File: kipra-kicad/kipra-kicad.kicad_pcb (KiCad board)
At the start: 2 copper layers, 128.2 x 134.8 mm, 51 parts

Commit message: add silkscreen text
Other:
- board text added: "k i p r a"
- board text added: "kipra v1 (2024-04) by Peter Lyons (focusaurus) It's kinda pragmatic."

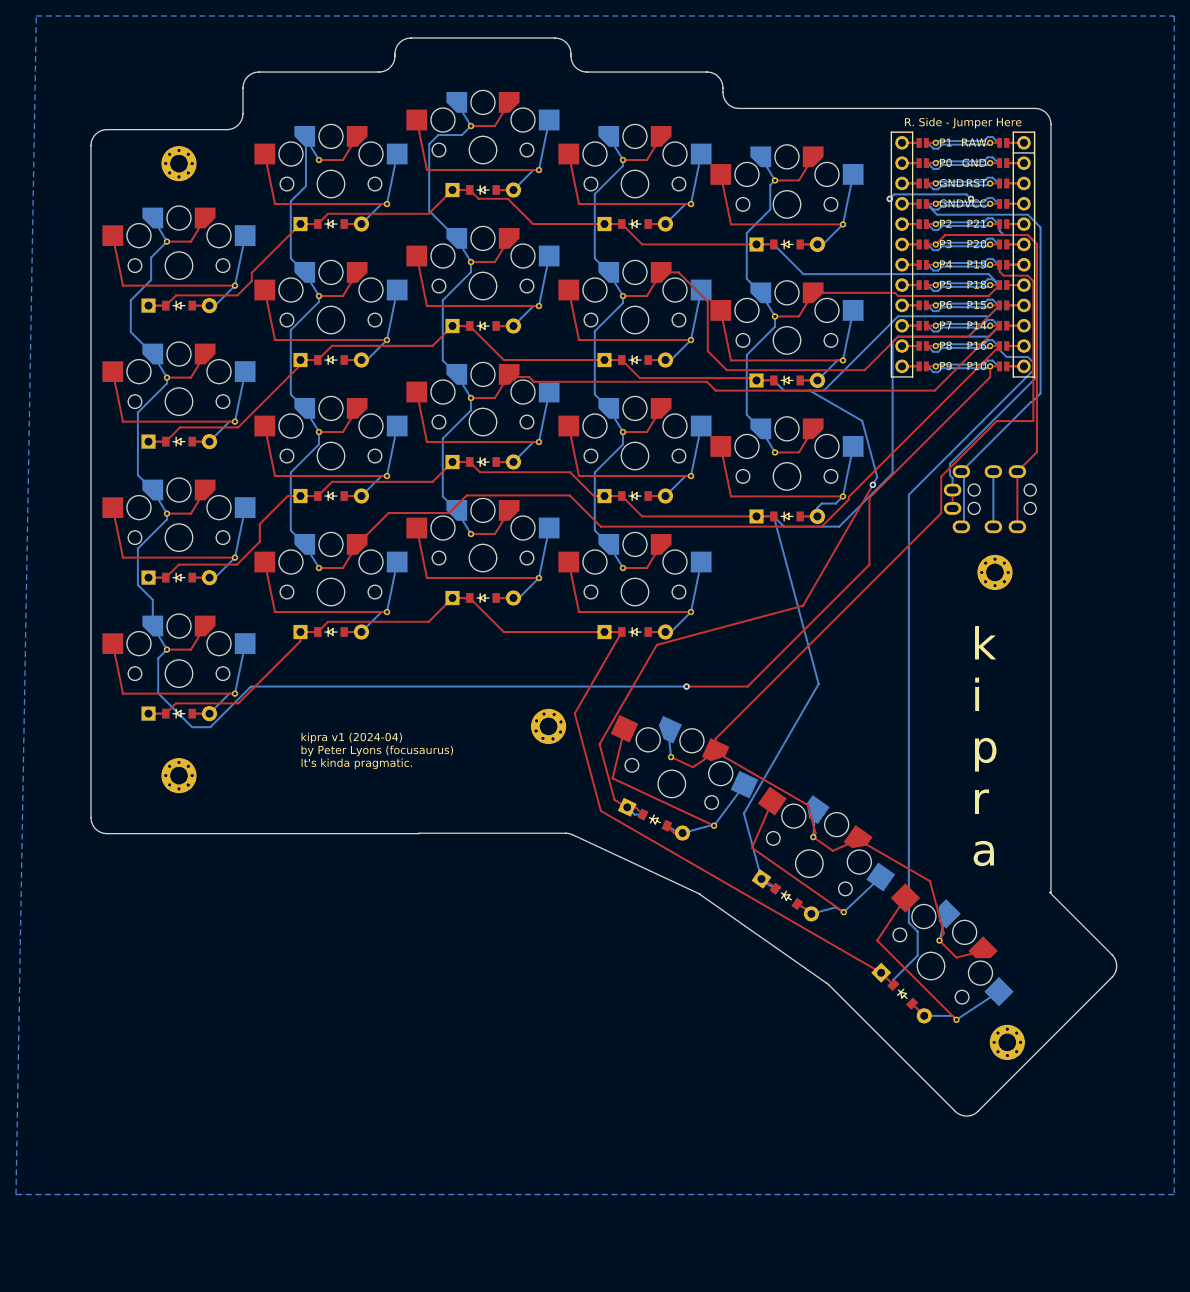
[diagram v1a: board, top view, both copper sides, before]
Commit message: added a reset button (ergogen redo)
Had to go back to ergogen. Will need to redo all the traces now.
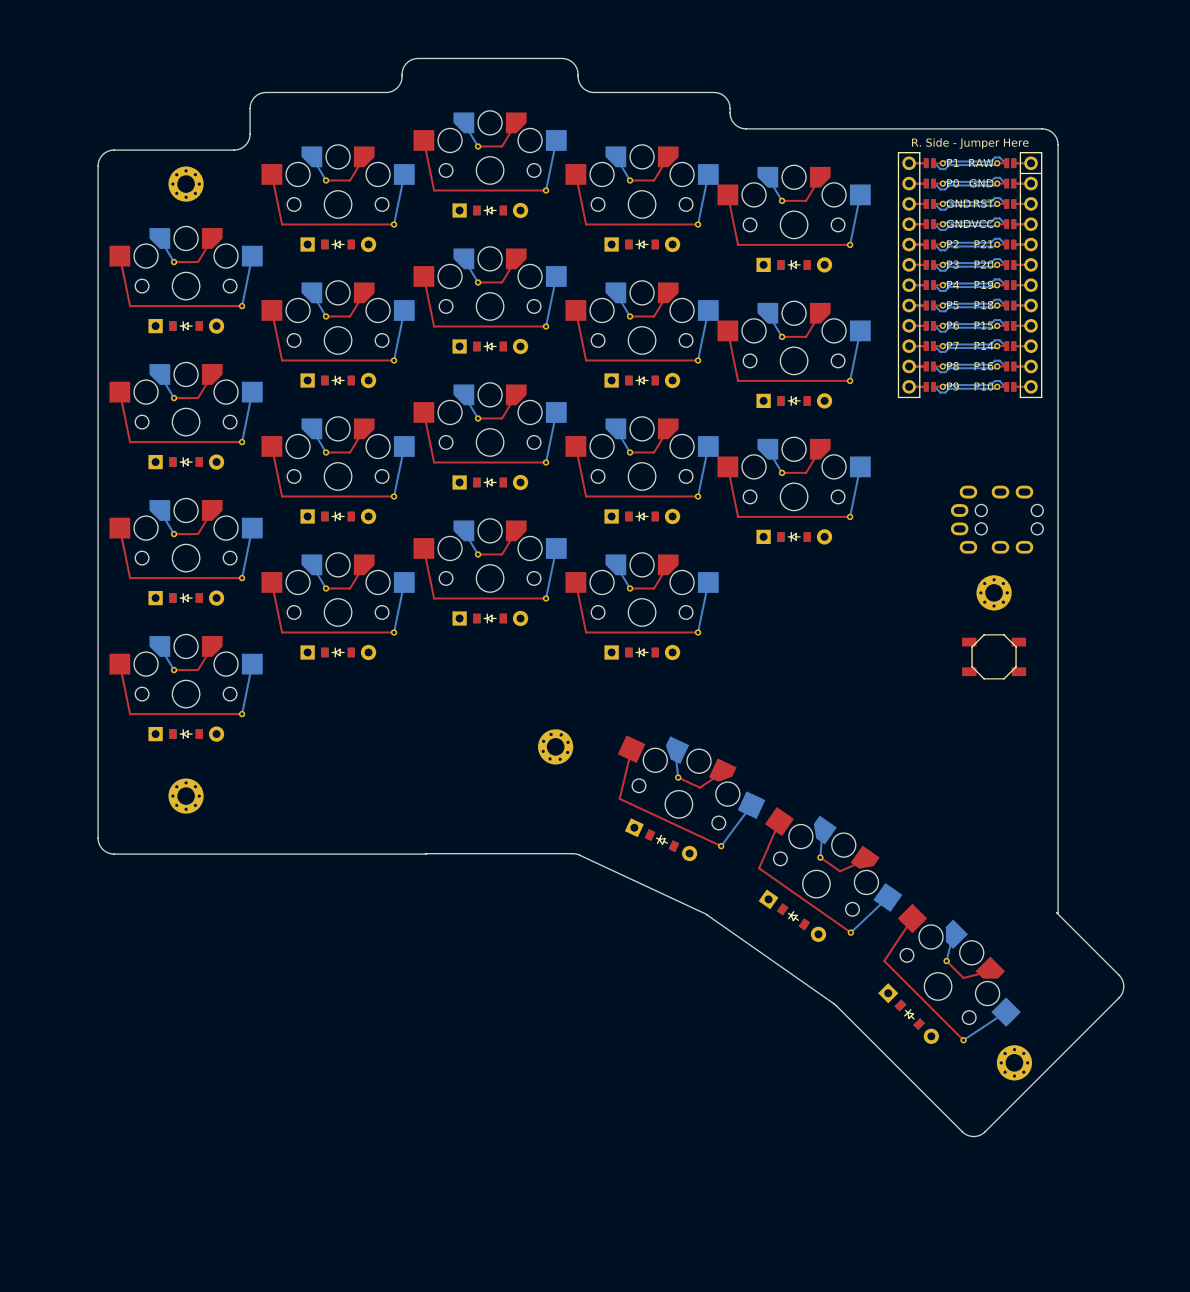
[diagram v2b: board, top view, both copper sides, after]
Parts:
- added B1: , E73:SW_TACT_ALPS_SKQGABE010, F.Cu at (201.0, 95.3)
- moved D16 2.71 mm to (157.0, 43.8)
- moved MCU1 2.71 mm to (198.0, 46.3)
- moved D11 2.71 mm to (138.0, 56.5)
- moved D15 2.71 mm to (157.0, 60.8)
- moved D2 2.71 mm to (100.0, 88.0)
- moved S17 2.71 mm to (176.0, 75.3)
- moved S6 2.71 mm to (119.0, 72.8)
- moved S3 2.71 mm to (100.0, 66.0)
- moved S4 2.71 mm to (100.0, 49.0)
- moved D7 2.71 mm to (119.0, 60.8)
- moved S16 2.71 mm to (157.0, 38.8)
- moved _1 2.71 mm to (100.0, 112.8)
- moved S12 2.71 mm to (138.0, 34.5)
- moved _2 2.71 mm to (100.0, 36.2)
- moved D12 2.71 mm to (138.0, 39.5)
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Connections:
- MCU1 pad 1: MCU1_1 -> RAW
- MCU1 pad 10: MCU1_10 -> P14
- MCU1 pad 11: MCU1_11 -> P16
- MCU1 pad 12: MCU1_12 -> P10
- MCU1 pad 2: MCU1_2 -> GND
- MCU1 pad 3: MCU1_3 -> RST
- MCU1 pad 4: MCU1_4 -> VCC
- MCU1 pad 5: MCU1_5 -> P21
- MCU1 pad 6: MCU1_6 -> P20
- MCU1 pad 7: MCU1_7 -> P19
- MCU1 pad 8: MCU1_8 -> P18
- MCU1 pad 9: MCU1_9 -> P15
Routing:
- net (no net): track 0.00 -> 806.3 mm
- net P8: track 246.3 -> 0.00 mm
- net P6: track 221.6 -> 0.00 mm, vias 1 -> 0
- net P10: track 234.9 -> 14.2 mm, vias 1 -> 0
- net P7: track 211.3 -> 0.00 mm
- net P16: track 194.2 -> 0.00 mm
- net P14: track 166.8 -> 0.00 mm
- net P19: track 158.5 -> 0.00 mm
- net P15: track 152.2 -> 0.00 mm
- net P5: track 138.3 -> 0.00 mm
- net P18: track 95.8 -> 0.00 mm
- net VCC: track 67.0 -> 0.00 mm
- net index_four: track 35.3 -> 101.6 mm
- net pinky_one: track 35.3 -> 101.4 mm
- net P3: track 59.6 -> 0.00 mm
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- removed copper zone on B.Cu, net GND
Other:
- outline, holes or cut-outs redrawn
- net class Default added: clearance 0.2, trace_width 0.25, via_dia 0.8, via_drill 0.4
- board text removed: "k i p r a"
- board text removed: "kipra v1 (2024-04) by Peter Lyons (focusaurus) It's kinda pragmatic."

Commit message: checkpoint before starting over to move row pins down one slot to the corner
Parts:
- moved D11 2.84 mm to (138.0, 53.7)
- moved TRRS1 2.84 mm to (208.0, 76.5)
- moved D21 2.84 mm to (175.9, 125.0)
- moved S21 2.84 mm to (178.8, 120.9)
- moved D12 2.84 mm to (138.0, 36.7)
- moved D16 2.84 mm to (157.0, 41.0)
- moved S20 2.84 mm to (194.0, 133.7)
- moved S3 2.84 mm to (100.0, 63.2)
- moved D17 2.84 mm to (176.0, 77.5)
- moved S18 2.84 mm to (176.0, 55.5)
- moved S17 2.84 mm to (176.0, 72.5)
- moved D14 2.84 mm to (157.0, 75.0)
- moved D2 2.84 mm to (100.0, 85.2)
- moved S19 2.84 mm to (176.0, 38.5)
- moved _1 2.84 mm to (100.0, 109.9)
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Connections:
- MCU1 pad 1: RAW -> MCU1_1
- MCU1 pad 10: P14 -> MCU1_10
- MCU1 pad 11: P16 -> MCU1_11
- MCU1 pad 12: P10 -> MCU1_12
- MCU1 pad 2: GND -> MCU1_2
- MCU1 pad 3: RST -> MCU1_3
- MCU1 pad 4: VCC -> MCU1_4
- MCU1 pad 5: P21 -> MCU1_5
- MCU1 pad 6: P20 -> MCU1_6
- MCU1 pad 7: P19 -> MCU1_7
- MCU1 pad 8: P18 -> MCU1_8
- MCU1 pad 9: P15 -> MCU1_9
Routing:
- net (no net): track 806.3 -> 0.00 mm
- net P6: track 0.00 -> 274.8 mm, vias 0 -> 1
- net P8: track 0.00 -> 253.8 mm
- net P10: track 14.2 -> 240.8 mm, vias 0 -> 2
- net P16: track 0.00 -> 209.8 mm
- net P7: track 0.00 -> 198.4 mm, vias 0 -> 1
- net P19: track 0.00 -> 186.6 mm
- net P14: track 0.00 -> 157.3 mm, vias 0 -> 1
- net P18: track 0.00 -> 147.6 mm
- net P15: track 0.00 -> 133.1 mm, vias 0 -> 1
- net P5: track 0.00 -> 132.6 mm
- net RST: track 0.00 -> 103.9 mm, vias 0 -> 3
- net VCC: track 0.00 -> 75.9 mm, vias 0 -> 1
- net index_four: track 101.6 -> 35.3 mm
- net pinky_one: track 101.4 -> 35.3 mm
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- added copper zone on B.Cu, net GND
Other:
- outline, holes or cut-outs redrawn
- net class Default removed
- board text added: "P2"

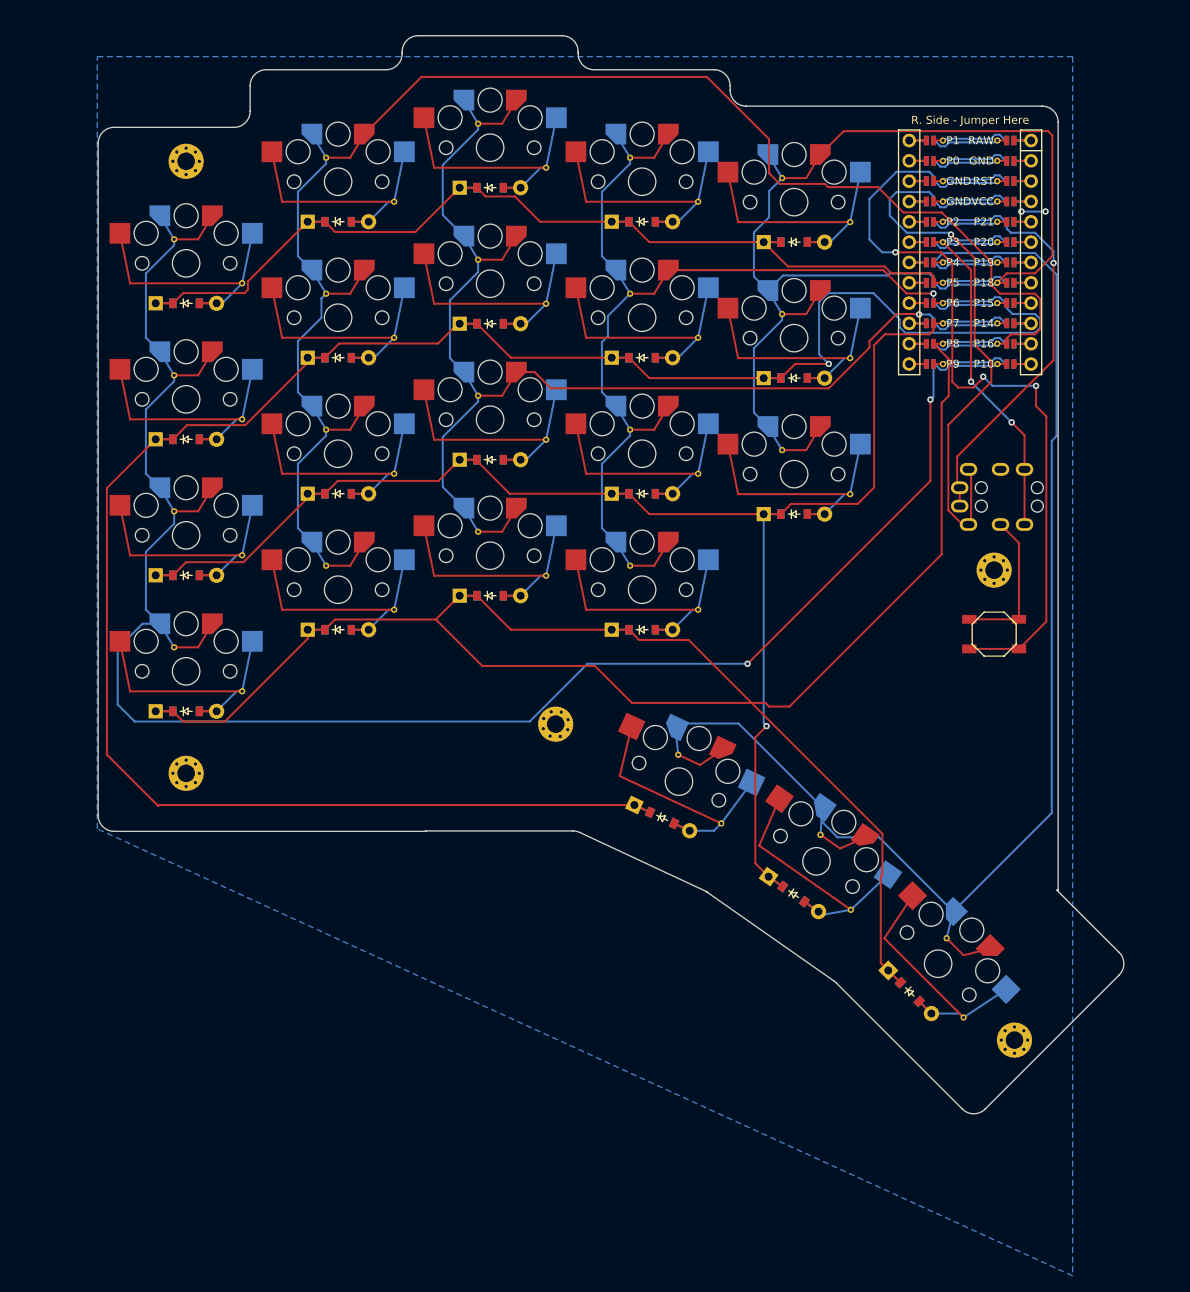
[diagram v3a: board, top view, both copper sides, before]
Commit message: cleaned up tracks. no DRC errors.
Paired with Jesse and Charles from Recurse Center
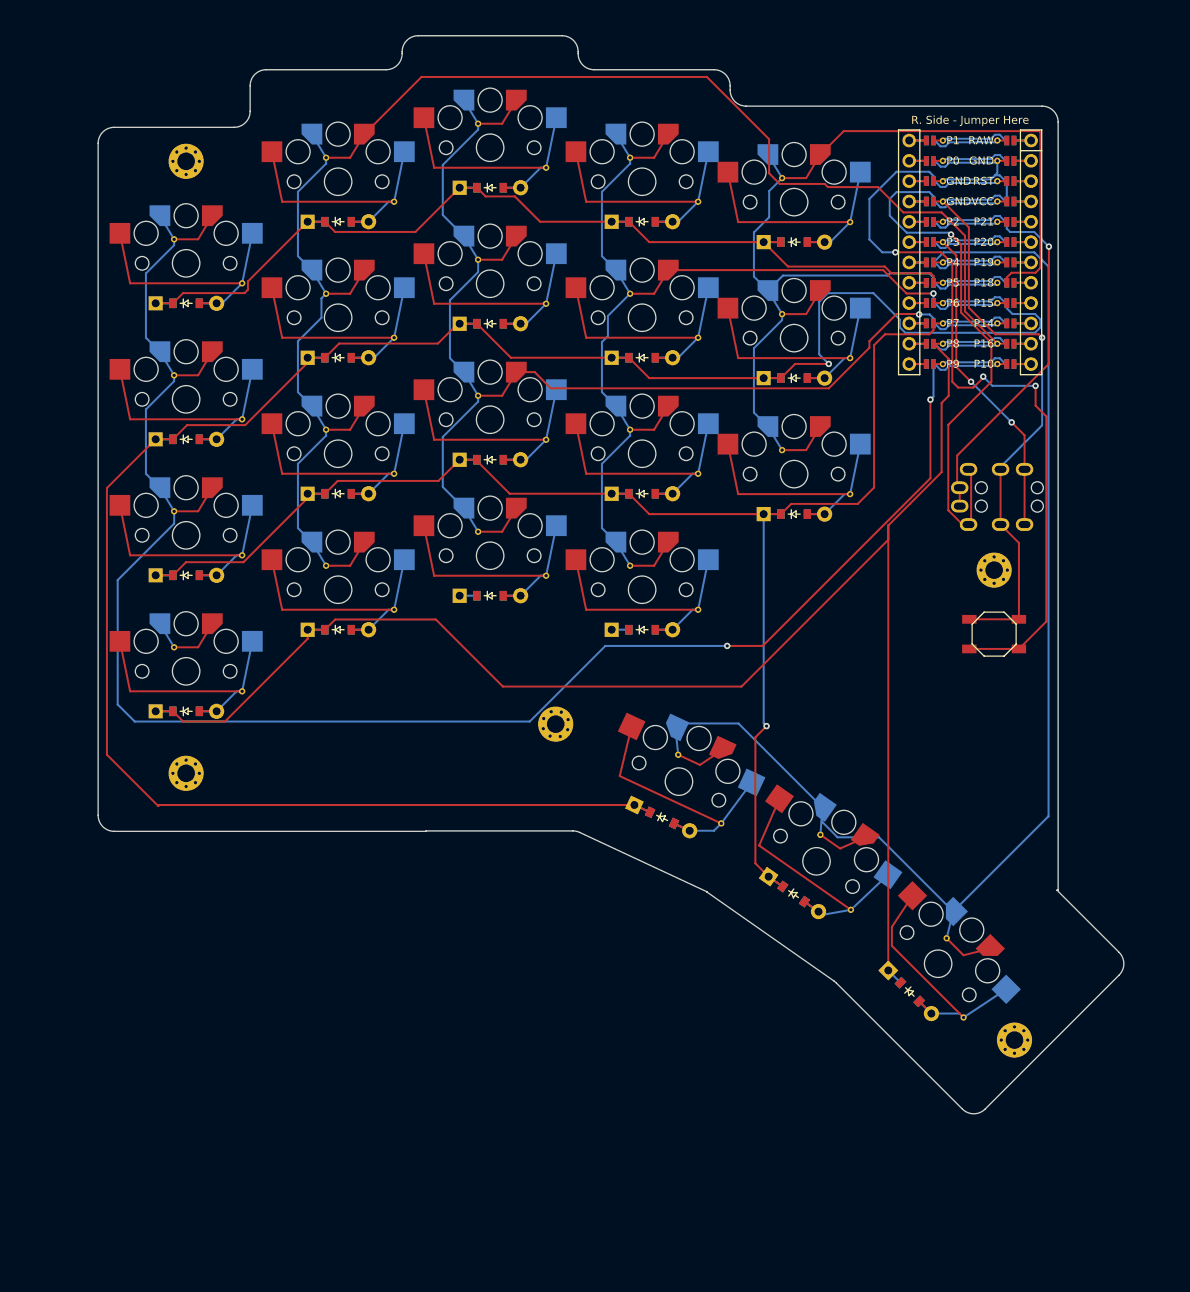
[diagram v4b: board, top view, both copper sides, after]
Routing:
- net GND: track 49.9 -> 102.2 mm, vias 2 -> 1
- net P8: track 253.8 -> 213.3 mm
- net P16: track 209.8 -> 201.5 mm
- net P18: track 147.6 -> 143.8 mm
- net P10: track 240.8 -> 237.9 mm
- net P19: track 186.6 -> 185.9 mm
- net thumb_far: track 35.3 -> 34.6 mm
- removed copper zone on B.Cu, net GND

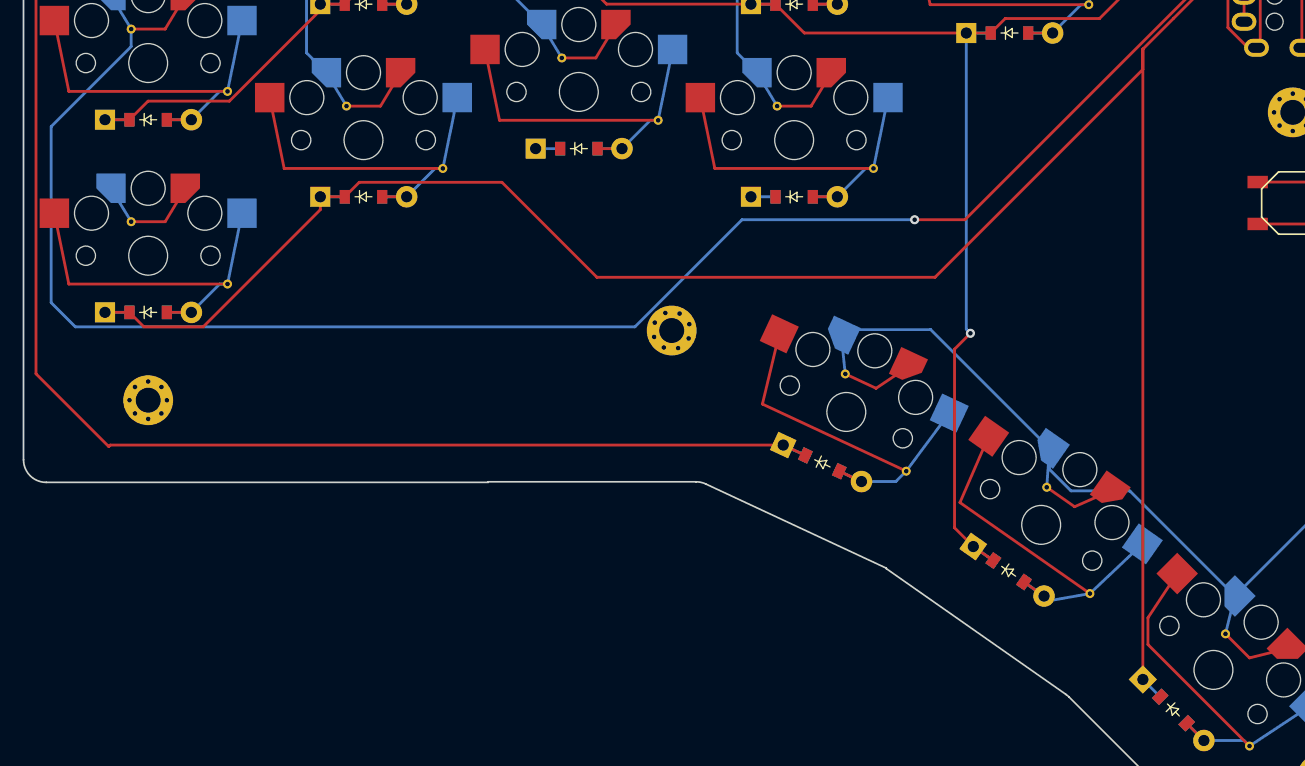
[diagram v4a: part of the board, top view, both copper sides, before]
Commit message: added silkscreen text
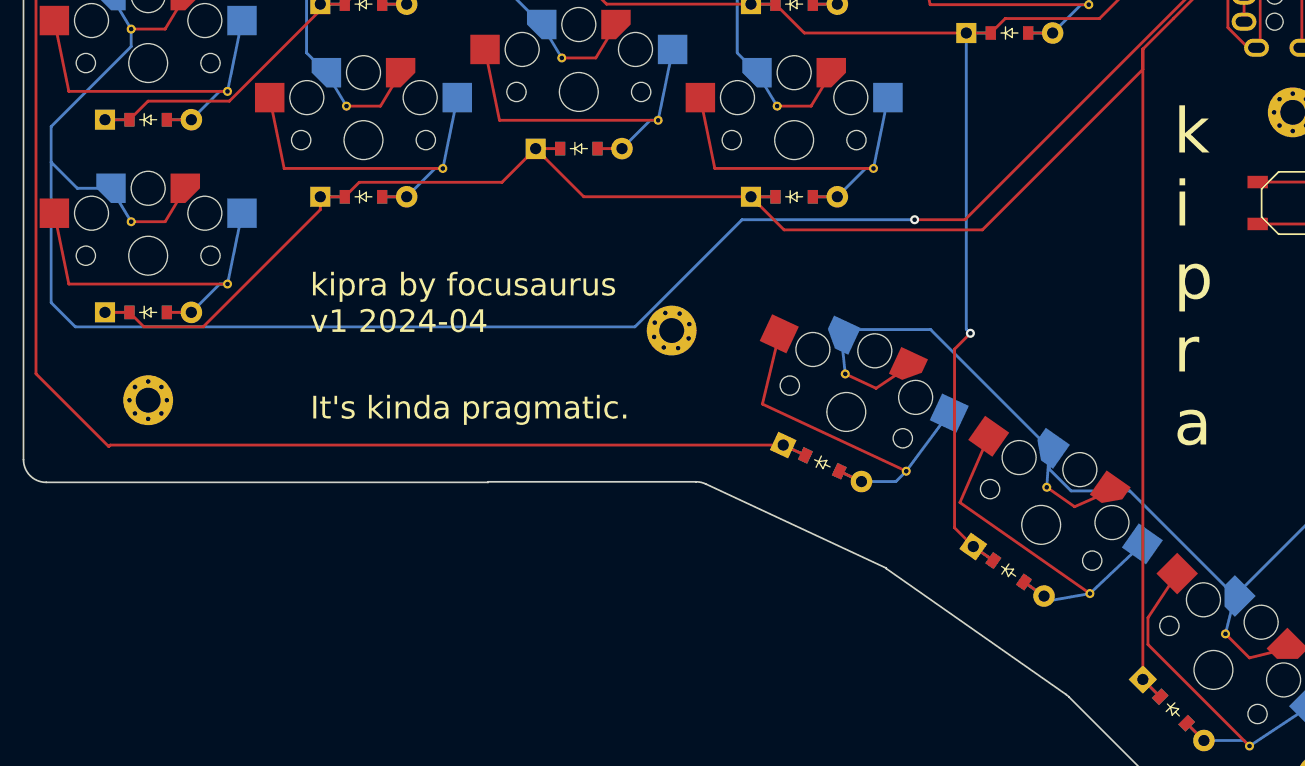
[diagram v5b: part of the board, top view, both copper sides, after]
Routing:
- net P10: track 237.9 -> 244.1 mm
- net P8: track 213.3 -> 219.2 mm
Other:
- board text added: "It's kinda pragmatic."
- board text added: "k i p r a"
- board text added: "kipra by focusaurus v1 2024-04"
